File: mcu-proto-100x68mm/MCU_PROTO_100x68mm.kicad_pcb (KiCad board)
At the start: 2 copper layers, 90 x 58 mm, 836 parts, among them J1 Screw_Terminal_01x04, J2 Screw_Terminal_01x04, J3 Conn_01x01_Pin, J4 Conn_01x01_Pin

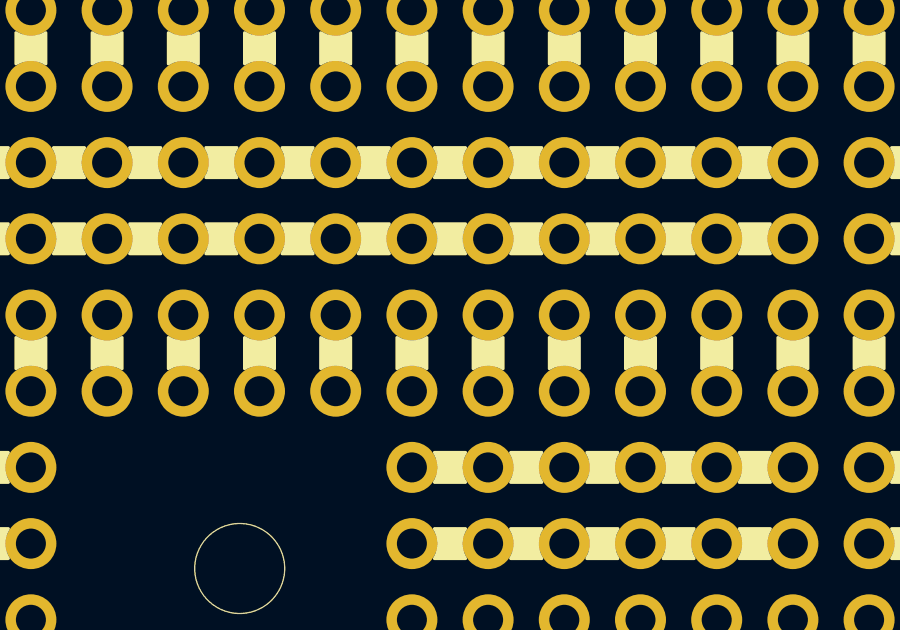
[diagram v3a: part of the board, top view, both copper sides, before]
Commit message: Silks in back plate
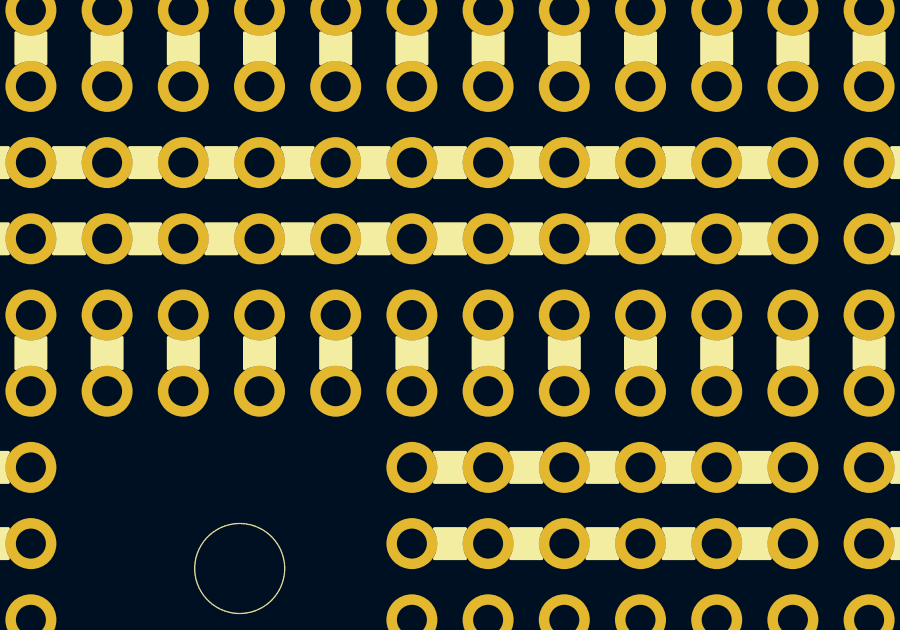
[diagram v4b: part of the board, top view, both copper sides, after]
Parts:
- added REF**310: Pad_Link_1.7mm_Width_1.0mm, proto-pcb-silks:PadLink_1.7mm_Width_1.0mm, B.Cu at (113.0, 105.5)
- added REF**311: Pad_Link_1.7mm_Width_1.0mm, proto-pcb-silks:PadLink_1.7mm_Width_1.0mm, B.Cu at (115.5, 105.5)
- added REF**312: Pad_Link_1.7mm_Width_1.0mm, proto-pcb-silks:PadLink_1.7mm_Width_1.0mm, B.Cu at (118.1, 105.5)
- added REF**318: Pad_Link_1.7mm_Width_1.0mm, proto-pcb-silks:PadLink_1.7mm_Width_1.0mm, B.Cu at (120.6, 105.5)
- added REF**353: Pad_Link_1.7mm_Width_1.0mm, proto-pcb-silks:PadLink_1.7mm_Width_1.0mm, B.Cu at (123.2, 105.5)
- added REF**354: Pad_Link_1.7mm_Width_1.0mm, proto-pcb-silks:PadLink_1.7mm_Width_1.0mm, B.Cu at (125.7, 105.5)
- added REF**355: Pad_Link_1.7mm_Width_1.0mm, proto-pcb-silks:PadLink_1.7mm_Width_1.0mm, B.Cu at (128.2, 105.5)
- added REF**356: Pad_Link_1.7mm_Width_1.0mm, proto-pcb-silks:PadLink_1.7mm_Width_1.0mm, B.Cu at (130.8, 105.5)
- added REF**357: Pad_Link_1.7mm_Width_1.0mm, proto-pcb-silks:PadLink_1.7mm_Width_1.0mm, B.Cu at (133.3, 105.5)
- added REF**358: Pad_Link_1.7mm_Width_1.0mm, proto-pcb-silks:PadLink_1.7mm_Width_1.0mm, B.Cu at (135.9, 105.5)
- added REF**359: Pad_Link_1.7mm_Width_1.0mm, proto-pcb-silks:PadLink_1.7mm_Width_1.0mm, B.Cu at (138.4, 105.5)
- added REF**360: Pad_Link_1.7mm_Width_1.0mm, proto-pcb-silks:PadLink_1.7mm_Width_1.0mm, B.Cu at (140.9, 105.5)
- added REF**361: Pad_Link_1.7mm_Width_1.0mm, proto-pcb-silks:PadLink_1.7mm_Width_1.0mm, B.Cu at (143.5, 105.5)
- added REF**362: Pad_Link_1.7mm_Width_1.0mm, proto-pcb-silks:PadLink_1.7mm_Width_1.0mm, B.Cu at (146.0, 105.5)
- added REF**363: Pad_Link_1.7mm_Width_1.0mm, proto-pcb-silks:PadLink_1.7mm_Width_1.0mm, B.Cu at (148.6, 105.5)
- added REF**364: Pad_Link_1.7mm_Width_1.0mm, proto-pcb-silks:PadLink_1.7mm_Width_1.0mm, B.Cu at (151.1, 105.5)
- added REF**365: Pad_Link_1.7mm_Width_1.0mm, proto-pcb-silks:PadLink_1.7mm_Width_1.0mm, B.Cu at (153.6, 105.5)
- added REF**366: Pad_Link_1.7mm_Width_1.0mm, proto-pcb-silks:PadLink_1.7mm_Width_1.0mm, B.Cu at (156.2, 105.5)
- added REF**367: Pad_Link_1.7mm_Width_1.0mm, proto-pcb-silks:PadLink_1.7mm_Width_1.0mm, B.Cu at (158.7, 105.5)
- added REF**368: Pad_Link_1.7mm_Width_1.0mm, proto-pcb-silks:PadLink_1.7mm_Width_1.0mm, B.Cu at (161.3, 105.5)
- added REF**369: Pad_Link_1.7mm_Width_1.0mm, proto-pcb-silks:PadLink_1.7mm_Width_1.0mm, B.Cu at (113.0, 108.0)
- added REF**370: Pad_Link_1.7mm_Width_1.0mm, proto-pcb-silks:PadLink_1.7mm_Width_1.0mm, B.Cu at (115.5, 108.0)
- added REF**371: Pad_Link_1.7mm_Width_1.0mm, proto-pcb-silks:PadLink_1.7mm_Width_1.0mm, B.Cu at (118.1, 108.0)
- added REF**372: Pad_Link_1.7mm_Width_1.0mm, proto-pcb-silks:PadLink_1.7mm_Width_1.0mm, B.Cu at (120.6, 108.0)
- added REF**373: Pad_Link_1.7mm_Width_1.0mm, proto-pcb-silks:PadLink_1.7mm_Width_1.0mm, B.Cu at (123.2, 108.0)
- added REF**374: Pad_Link_1.7mm_Width_1.0mm, proto-pcb-silks:PadLink_1.7mm_Width_1.0mm, B.Cu at (125.7, 108.0)
- added REF**375: Pad_Link_1.7mm_Width_1.0mm, proto-pcb-silks:PadLink_1.7mm_Width_1.0mm, B.Cu at (128.2, 108.0)
- added REF**376: Pad_Link_1.7mm_Width_1.0mm, proto-pcb-silks:PadLink_1.7mm_Width_1.0mm, B.Cu at (130.8, 108.0)
- added REF**377: Pad_Link_1.7mm_Width_1.0mm, proto-pcb-silks:PadLink_1.7mm_Width_1.0mm, B.Cu at (133.3, 108.0)
- added REF**378: Pad_Link_1.7mm_Width_1.0mm, proto-pcb-silks:PadLink_1.7mm_Width_1.0mm, B.Cu at (135.9, 108.0)
- added REF**379: Pad_Link_1.7mm_Width_1.0mm, proto-pcb-silks:PadLink_1.7mm_Width_1.0mm, B.Cu at (138.4, 108.0)
- added REF**380: Pad_Link_1.7mm_Width_1.0mm, proto-pcb-silks:PadLink_1.7mm_Width_1.0mm, B.Cu at (140.9, 108.0)
- added REF**381: Pad_Link_1.7mm_Width_1.0mm, proto-pcb-silks:PadLink_1.7mm_Width_1.0mm, B.Cu at (143.5, 108.0)
- added REF**382: Pad_Link_1.7mm_Width_1.0mm, proto-pcb-silks:PadLink_1.7mm_Width_1.0mm, B.Cu at (146.0, 108.0)
- added REF**383: Pad_Link_1.7mm_Width_1.0mm, proto-pcb-silks:PadLink_1.7mm_Width_1.0mm, B.Cu at (148.6, 108.0)
- added REF**384: Pad_Link_1.7mm_Width_1.0mm, proto-pcb-silks:PadLink_1.7mm_Width_1.0mm, B.Cu at (151.1, 108.0)
- added REF**385: Pad_Link_1.7mm_Width_1.0mm, proto-pcb-silks:PadLink_1.7mm_Width_1.0mm, B.Cu at (153.6, 108.0)
- added REF**386: Pad_Link_1.7mm_Width_1.0mm, proto-pcb-silks:PadLink_1.7mm_Width_1.0mm, B.Cu at (156.2, 108.0)
- added REF**387: Pad_Link_1.7mm_Width_1.0mm, proto-pcb-silks:PadLink_1.7mm_Width_1.0mm, B.Cu at (158.7, 108.0)
- added REF**388: Pad_Link_1.7mm_Width_1.0mm, proto-pcb-silks:PadLink_1.7mm_Width_1.0mm, B.Cu at (161.3, 108.0)
- added REF**389: Pad_Link_1.7mm_Width_1.0mm, proto-pcb-silks:PadLink_1.7mm_Width_1.0mm, B.Cu at (113.0, 113.1)
- added REF**390: Pad_Link_1.7mm_Width_1.0mm, proto-pcb-silks:PadLink_1.7mm_Width_1.0mm, B.Cu at (115.5, 113.1)
- added REF**391: Pad_Link_1.7mm_Width_1.0mm, proto-pcb-silks:PadLink_1.7mm_Width_1.0mm, B.Cu at (118.1, 113.1)
- added REF**392: Pad_Link_1.7mm_Width_1.0mm, proto-pcb-silks:PadLink_1.7mm_Width_1.0mm, B.Cu at (120.6, 113.1)
- added REF**393: Pad_Link_1.7mm_Width_1.0mm, proto-pcb-silks:PadLink_1.7mm_Width_1.0mm, B.Cu at (123.2, 113.1)
- added REF**394: Pad_Link_1.7mm_Width_1.0mm, proto-pcb-silks:PadLink_1.7mm_Width_1.0mm, B.Cu at (125.7, 113.1)
- added REF**395: Pad_Link_1.7mm_Width_1.0mm, proto-pcb-silks:PadLink_1.7mm_Width_1.0mm, B.Cu at (128.2, 113.1)
- added REF**396: Pad_Link_1.7mm_Width_1.0mm, proto-pcb-silks:PadLink_1.7mm_Width_1.0mm, B.Cu at (130.8, 113.1)
- added REF**397: Pad_Link_1.7mm_Width_1.0mm, proto-pcb-silks:PadLink_1.7mm_Width_1.0mm, B.Cu at (133.3, 113.1)
- added REF**398: Pad_Link_1.7mm_Width_1.0mm, proto-pcb-silks:PadLink_1.7mm_Width_1.0mm, B.Cu at (135.9, 113.1)
- added REF**399: Pad_Link_1.7mm_Width_1.0mm, proto-pcb-silks:PadLink_1.7mm_Width_1.0mm, B.Cu at (138.4, 113.1)
- added REF**400: Pad_Link_1.7mm_Width_1.0mm, proto-pcb-silks:PadLink_1.7mm_Width_1.0mm, B.Cu at (140.9, 113.1)
- added REF**401: Pad_Link_1.7mm_Width_1.0mm, proto-pcb-silks:PadLink_1.7mm_Width_1.0mm, B.Cu at (143.5, 113.1)
- added REF**402: Pad_Link_1.7mm_Width_1.0mm, proto-pcb-silks:PadLink_1.7mm_Width_1.0mm, B.Cu at (146.0, 113.1)
- added REF**403: Pad_Link_1.7mm_Width_1.0mm, proto-pcb-silks:PadLink_1.7mm_Width_1.0mm, B.Cu at (148.6, 113.1)
- added REF**404: Pad_Link_1.7mm_Width_1.0mm, proto-pcb-silks:PadLink_1.7mm_Width_1.0mm, B.Cu at (151.1, 113.1)
- added REF**405: Pad_Link_1.7mm_Width_1.0mm, proto-pcb-silks:PadLink_1.7mm_Width_1.0mm, B.Cu at (153.6, 113.1)
- added REF**406: Pad_Link_1.7mm_Width_1.0mm, proto-pcb-silks:PadLink_1.7mm_Width_1.0mm, B.Cu at (156.2, 113.1)
- added REF**407: Pad_Link_1.7mm_Width_1.0mm, proto-pcb-silks:PadLink_1.7mm_Width_1.0mm, B.Cu at (158.7, 113.1)
- added REF**408: Pad_Link_1.7mm_Width_1.0mm, proto-pcb-silks:PadLink_1.7mm_Width_1.0mm, B.Cu at (161.3, 113.1)
- added REF**409: Pad_Link_1.7mm_Width_1.0mm, proto-pcb-silks:PadLink_1.7mm_Width_1.0mm, B.Cu at (113.0, 115.6)
- added REF**410: Pad_Link_1.7mm_Width_1.0mm, proto-pcb-silks:PadLink_1.7mm_Width_1.0mm, B.Cu at (115.5, 115.6)
- added REF**411: Pad_Link_1.7mm_Width_1.0mm, proto-pcb-silks:PadLink_1.7mm_Width_1.0mm, B.Cu at (118.1, 115.6)
- added REF**412: Pad_Link_1.7mm_Width_1.0mm, proto-pcb-silks:PadLink_1.7mm_Width_1.0mm, B.Cu at (120.6, 115.6)
- added REF**413: Pad_Link_1.7mm_Width_1.0mm, proto-pcb-silks:PadLink_1.7mm_Width_1.0mm, B.Cu at (123.2, 115.6)
- added REF**414: Pad_Link_1.7mm_Width_1.0mm, proto-pcb-silks:PadLink_1.7mm_Width_1.0mm, B.Cu at (125.7, 115.6)
- added REF**415: Pad_Link_1.7mm_Width_1.0mm, proto-pcb-silks:PadLink_1.7mm_Width_1.0mm, B.Cu at (128.2, 115.6)
- added REF**416: Pad_Link_1.7mm_Width_1.0mm, proto-pcb-silks:PadLink_1.7mm_Width_1.0mm, B.Cu at (130.8, 115.6)
- added REF**417: Pad_Link_1.7mm_Width_1.0mm, proto-pcb-silks:PadLink_1.7mm_Width_1.0mm, B.Cu at (133.3, 115.6)
- added REF**418: Pad_Link_1.7mm_Width_1.0mm, proto-pcb-silks:PadLink_1.7mm_Width_1.0mm, B.Cu at (135.9, 115.6)
- added REF**419: Pad_Link_1.7mm_Width_1.0mm, proto-pcb-silks:PadLink_1.7mm_Width_1.0mm, B.Cu at (138.4, 115.6)
- added REF**420: Pad_Link_1.7mm_Width_1.0mm, proto-pcb-silks:PadLink_1.7mm_Width_1.0mm, B.Cu at (113.0, 123.2)
- added REF**421: Pad_Link_1.7mm_Width_1.0mm, proto-pcb-silks:PadLink_1.7mm_Width_1.0mm, B.Cu at (143.5, 115.6)
- added REF**422: Pad_Link_1.7mm_Width_1.0mm, proto-pcb-silks:PadLink_1.7mm_Width_1.0mm, B.Cu at (146.0, 115.6)
- added REF**423: Pad_Link_1.7mm_Width_1.0mm, proto-pcb-silks:PadLink_1.7mm_Width_1.0mm, B.Cu at (148.6, 115.6)
- added REF**424: Pad_Link_1.7mm_Width_1.0mm, proto-pcb-silks:PadLink_1.7mm_Width_1.0mm, B.Cu at (151.1, 115.6)
- added REF**425: Pad_Link_1.7mm_Width_1.0mm, proto-pcb-silks:PadLink_1.7mm_Width_1.0mm, B.Cu at (153.6, 115.6)
- added REF**426: Pad_Link_1.7mm_Width_1.0mm, proto-pcb-silks:PadLink_1.7mm_Width_1.0mm, B.Cu at (156.2, 115.6)
- added REF**427: Pad_Link_1.7mm_Width_1.0mm, proto-pcb-silks:PadLink_1.7mm_Width_1.0mm, B.Cu at (158.7, 115.6)
- added REF**428: Pad_Link_1.7mm_Width_1.0mm, proto-pcb-silks:PadLink_1.7mm_Width_1.0mm, B.Cu at (161.3, 115.6)
- added REF**429: Pad_Link_1.7mm_Width_1.0mm, proto-pcb-silks:PadLink_1.7mm_Width_1.0mm, B.Cu at (163.8, 115.6)
- added REF**430: Pad_Link_1.7mm_Width_1.0mm, proto-pcb-silks:PadLink_1.7mm_Width_1.0mm, B.Cu at (166.3, 115.6)
- added REF**431: Pad_Link_1.7mm_Width_1.0mm, proto-pcb-silks:PadLink_1.7mm_Width_1.0mm, B.Cu at (113.0, 118.2)
- added REF**432: Pad_Link_1.7mm_Width_1.0mm, proto-pcb-silks:PadLink_1.7mm_Width_1.0mm, B.Cu at (115.5, 118.2)
- added REF**433: Pad_Link_1.7mm_Width_1.0mm, proto-pcb-silks:PadLink_1.7mm_Width_1.0mm, B.Cu at (118.1, 118.2)
- added REF**434: Pad_Link_1.7mm_Width_1.0mm, proto-pcb-silks:PadLink_1.7mm_Width_1.0mm, B.Cu at (120.6, 118.2)
- added REF**435: Pad_Link_1.7mm_Width_1.0mm, proto-pcb-silks:PadLink_1.7mm_Width_1.0mm, B.Cu at (123.2, 118.2)
- added REF**436: Pad_Link_1.7mm_Width_1.0mm, proto-pcb-silks:PadLink_1.7mm_Width_1.0mm, B.Cu at (125.7, 118.2)
- added REF**437: Pad_Link_1.7mm_Width_1.0mm, proto-pcb-silks:PadLink_1.7mm_Width_1.0mm, B.Cu at (128.2, 118.2)
- added REF**438: Pad_Link_1.7mm_Width_1.0mm, proto-pcb-silks:PadLink_1.7mm_Width_1.0mm, B.Cu at (130.8, 118.2)
- added REF**439: Pad_Link_1.7mm_Width_1.0mm, proto-pcb-silks:PadLink_1.7mm_Width_1.0mm, B.Cu at (133.3, 118.2)
- added REF**440: Pad_Link_1.7mm_Width_1.0mm, proto-pcb-silks:PadLink_1.7mm_Width_1.0mm, B.Cu at (135.9, 118.2)
- added REF**441: Pad_Link_1.7mm_Width_1.0mm, proto-pcb-silks:PadLink_1.7mm_Width_1.0mm, B.Cu at (138.4, 118.2)
- added REF**442: Pad_Link_1.7mm_Width_1.0mm, proto-pcb-silks:PadLink_1.7mm_Width_1.0mm, B.Cu at (115.5, 123.2)
- added REF**443: Pad_Link_1.7mm_Width_1.0mm, proto-pcb-silks:PadLink_1.7mm_Width_1.0mm, B.Cu at (143.5, 118.2)
- added REF**444: Pad_Link_1.7mm_Width_1.0mm, proto-pcb-silks:PadLink_1.7mm_Width_1.0mm, B.Cu at (146.0, 118.2)
- added REF**445: Pad_Link_1.7mm_Width_1.0mm, proto-pcb-silks:PadLink_1.7mm_Width_1.0mm, B.Cu at (148.6, 118.2)
- added REF**446: Pad_Link_1.7mm_Width_1.0mm, proto-pcb-silks:PadLink_1.7mm_Width_1.0mm, B.Cu at (151.1, 118.2)
- added REF**447: Pad_Link_1.7mm_Width_1.0mm, proto-pcb-silks:PadLink_1.7mm_Width_1.0mm, B.Cu at (153.6, 118.2)
- added REF**448: Pad_Link_1.7mm_Width_1.0mm, proto-pcb-silks:PadLink_1.7mm_Width_1.0mm, B.Cu at (156.2, 118.2)
- added REF**449: Pad_Link_1.7mm_Width_1.0mm, proto-pcb-silks:PadLink_1.7mm_Width_1.0mm, B.Cu at (158.7, 118.2)
- added REF**450: Pad_Link_1.7mm_Width_1.0mm, proto-pcb-silks:PadLink_1.7mm_Width_1.0mm, B.Cu at (161.3, 118.2)
- added REF**451: Pad_Link_1.7mm_Width_1.0mm, proto-pcb-silks:PadLink_1.7mm_Width_1.0mm, B.Cu at (163.8, 118.2)
- added REF**452: Pad_Link_1.7mm_Width_1.0mm, proto-pcb-silks:PadLink_1.7mm_Width_1.0mm, B.Cu at (166.3, 118.2)
- added REF**453: Pad_Link_1.7mm_Width_1.0mm, proto-pcb-silks:PadLink_1.7mm_Width_1.0mm, B.Cu at (118.1, 123.2)
- added REF**454: Pad_Link_1.7mm_Width_1.0mm, proto-pcb-silks:PadLink_1.7mm_Width_1.0mm, B.Cu at (120.6, 123.2)
- added REF**455: Pad_Link_1.7mm_Width_1.0mm, proto-pcb-silks:PadLink_1.7mm_Width_1.0mm, B.Cu at (123.2, 123.2)
- added REF**456: Pad_Link_1.7mm_Width_1.0mm, proto-pcb-silks:PadLink_1.7mm_Width_1.0mm, B.Cu at (125.7, 123.2)
- added REF**457: Pad_Link_1.7mm_Width_1.0mm, proto-pcb-silks:PadLink_1.7mm_Width_1.0mm, B.Cu at (128.2, 123.2)
- added REF**458: Pad_Link_1.7mm_Width_1.0mm, proto-pcb-silks:PadLink_1.7mm_Width_1.0mm, B.Cu at (130.8, 123.2)
- added REF**459: Pad_Link_1.7mm_Width_1.0mm, proto-pcb-silks:PadLink_1.7mm_Width_1.0mm, B.Cu at (133.3, 123.2)
- added REF**460: Pad_Link_1.7mm_Width_1.0mm, proto-pcb-silks:PadLink_1.7mm_Width_1.0mm, B.Cu at (135.9, 123.2)
- added REF**461: Pad_Link_1.7mm_Width_1.0mm, proto-pcb-silks:PadLink_1.7mm_Width_1.0mm, B.Cu at (138.4, 123.2)
- added REF**462: Pad_Link_1.7mm_Width_1.0mm, proto-pcb-silks:PadLink_1.7mm_Width_1.0mm, B.Cu at (140.9, 123.2)
- added REF**463: Pad_Link_1.7mm_Width_1.0mm, proto-pcb-silks:PadLink_1.7mm_Width_1.0mm, B.Cu at (143.5, 123.2)
- added REF**464: Pad_Link_1.7mm_Width_1.0mm, proto-pcb-silks:PadLink_1.7mm_Width_1.0mm, B.Cu at (146.0, 123.2)
- added REF**465: Pad_Link_1.7mm_Width_1.0mm, proto-pcb-silks:PadLink_1.7mm_Width_1.0mm, B.Cu at (148.6, 123.2)
- added REF**466: Pad_Link_1.7mm_Width_1.0mm, proto-pcb-silks:PadLink_1.7mm_Width_1.0mm, B.Cu at (151.1, 123.2)
- added REF**467: Pad_Link_1.7mm_Width_1.0mm, proto-pcb-silks:PadLink_1.7mm_Width_1.0mm, B.Cu at (153.6, 123.2)
- added REF**468: Pad_Link_1.7mm_Width_1.0mm, proto-pcb-silks:PadLink_1.7mm_Width_1.0mm, B.Cu at (156.2, 123.2)
- added REF**469: Pad_Link_1.7mm_Width_1.0mm, proto-pcb-silks:PadLink_1.7mm_Width_1.0mm, B.Cu at (158.7, 123.2)
- added REF**470: Pad_Link_1.7mm_Width_1.0mm, proto-pcb-silks:PadLink_1.7mm_Width_1.0mm, B.Cu at (161.3, 123.2)
- added REF**471: Pad_Link_1.7mm_Width_1.0mm, proto-pcb-silks:PadLink_1.7mm_Width_1.0mm, B.Cu at (163.8, 123.2)
- added REF**472: Pad_Link_1.7mm_Width_1.0mm, proto-pcb-silks:PadLink_1.7mm_Width_1.0mm, B.Cu at (166.3, 123.2)
- added REF**473: Pad_Link_1.7mm_Width_1.0mm, proto-pcb-silks:PadLink_1.7mm_Width_1.0mm, B.Cu at (168.9, 123.2)
- added REF**474: Pad_Link_1.7mm_Width_1.0mm, proto-pcb-silks:PadLink_1.7mm_Width_1.0mm, B.Cu at (113.0, 125.8)
- added REF**475: Pad_Link_1.7mm_Width_1.0mm, proto-pcb-silks:PadLink_1.7mm_Width_1.0mm, B.Cu at (115.5, 125.8)
- added REF**476: Pad_Link_1.7mm_Width_1.0mm, proto-pcb-silks:PadLink_1.7mm_Width_1.0mm, B.Cu at (118.1, 125.8)
- added REF**477: Pad_Link_1.7mm_Width_1.0mm, proto-pcb-silks:PadLink_1.7mm_Width_1.0mm, B.Cu at (120.6, 125.8)
- added REF**478: Pad_Link_1.7mm_Width_1.0mm, proto-pcb-silks:PadLink_1.7mm_Width_1.0mm, B.Cu at (123.2, 125.8)
- added REF**479: Pad_Link_1.7mm_Width_1.0mm, proto-pcb-silks:PadLink_1.7mm_Width_1.0mm, B.Cu at (125.7, 125.8)
- added REF**480: Pad_Link_1.7mm_Width_1.0mm, proto-pcb-silks:PadLink_1.7mm_Width_1.0mm, B.Cu at (128.2, 125.8)
- added REF**481: Pad_Link_1.7mm_Width_1.0mm, proto-pcb-silks:PadLink_1.7mm_Width_1.0mm, B.Cu at (130.8, 125.8)
- added REF**482: Pad_Link_1.7mm_Width_1.0mm, proto-pcb-silks:PadLink_1.7mm_Width_1.0mm, B.Cu at (133.3, 125.8)
- added REF**483: Pad_Link_1.7mm_Width_1.0mm, proto-pcb-silks:PadLink_1.7mm_Width_1.0mm, B.Cu at (135.9, 125.8)
- added REF**484: Pad_Link_1.7mm_Width_1.0mm, proto-pcb-silks:PadLink_1.7mm_Width_1.0mm, B.Cu at (138.4, 125.8)
- added REF**485: Pad_Link_1.7mm_Width_1.0mm, proto-pcb-silks:PadLink_1.7mm_Width_1.0mm, B.Cu at (140.9, 125.8)
- added REF**486: Pad_Link_1.7mm_Width_1.0mm, proto-pcb-silks:PadLink_1.7mm_Width_1.0mm, B.Cu at (143.5, 125.8)
- added REF**487: Pad_Link_1.7mm_Width_1.0mm, proto-pcb-silks:PadLink_1.7mm_Width_1.0mm, B.Cu at (146.0, 125.8)
- added REF**488: Pad_Link_1.7mm_Width_1.0mm, proto-pcb-silks:PadLink_1.7mm_Width_1.0mm, B.Cu at (148.6, 125.8)
- added REF**489: Pad_Link_1.7mm_Width_1.0mm, proto-pcb-silks:PadLink_1.7mm_Width_1.0mm, B.Cu at (151.1, 125.8)
- added REF**490: Pad_Link_1.7mm_Width_1.0mm, proto-pcb-silks:PadLink_1.7mm_Width_1.0mm, B.Cu at (153.6, 125.8)
- added REF**491: Pad_Link_1.7mm_Width_1.0mm, proto-pcb-silks:PadLink_1.7mm_Width_1.0mm, B.Cu at (156.2, 125.8)
- added REF**492: Pad_Link_1.7mm_Width_1.0mm, proto-pcb-silks:PadLink_1.7mm_Width_1.0mm, B.Cu at (158.7, 125.8)
- added REF**493: Pad_Link_1.7mm_Width_1.0mm, proto-pcb-silks:PadLink_1.7mm_Width_1.0mm, B.Cu at (161.3, 125.8)
- added REF**494: Pad_Link_1.7mm_Width_1.0mm, proto-pcb-silks:PadLink_1.7mm_Width_1.0mm, B.Cu at (163.8, 125.8)
- added REF**495: Pad_Link_1.7mm_Width_1.0mm, proto-pcb-silks:PadLink_1.7mm_Width_1.0mm, B.Cu at (166.3, 125.8)
- added REF**496: Pad_Link_1.7mm_Width_1.0mm, proto-pcb-silks:PadLink_1.7mm_Width_1.0mm, B.Cu at (168.9, 125.8)
- added REF**497: Pad_Link_1.7mm_Width_1.0mm, proto-pcb-silks:PadLink_1.7mm_Width_1.0mm, B.Cu at (113.0, 128.3)
- added REF**498: Pad_Link_1.7mm_Width_1.0mm, proto-pcb-silks:PadLink_1.7mm_Width_1.0mm, B.Cu at (115.5, 128.3)
- added REF**499: Pad_Link_1.7mm_Width_1.0mm, proto-pcb-silks:PadLink_1.7mm_Width_1.0mm, B.Cu at (118.1, 128.3)
- added REF**500: Pad_Link_1.7mm_Width_1.0mm, proto-pcb-silks:PadLink_1.7mm_Width_1.0mm, B.Cu at (120.6, 128.3)
- added REF**501: Pad_Link_1.7mm_Width_1.0mm, proto-pcb-silks:PadLink_1.7mm_Width_1.0mm, B.Cu at (123.2, 128.3)
- added REF**502: Pad_Link_1.7mm_Width_1.0mm, proto-pcb-silks:PadLink_1.7mm_Width_1.0mm, B.Cu at (125.7, 128.3)
- added REF**503: Pad_Link_1.7mm_Width_1.0mm, proto-pcb-silks:PadLink_1.7mm_Width_1.0mm, B.Cu at (128.2, 128.3)
- added REF**504: Pad_Link_1.7mm_Width_1.0mm, proto-pcb-silks:PadLink_1.7mm_Width_1.0mm, B.Cu at (130.8, 128.3)
- added REF**505: Pad_Link_1.7mm_Width_1.0mm, proto-pcb-silks:PadLink_1.7mm_Width_1.0mm, B.Cu at (133.3, 128.3)
- added REF**506: Pad_Link_1.7mm_Width_1.0mm, proto-pcb-silks:PadLink_1.7mm_Width_1.0mm, B.Cu at (135.9, 128.3)
- added REF**507: Pad_Link_1.7mm_Width_1.0mm, proto-pcb-silks:PadLink_1.7mm_Width_1.0mm, B.Cu at (138.4, 128.3)
- added REF**508: Pad_Link_1.7mm_Width_1.0mm, proto-pcb-silks:PadLink_1.7mm_Width_1.0mm, B.Cu at (140.9, 128.3)
- added REF**509: Pad_Link_1.7mm_Width_1.0mm, proto-pcb-silks:PadLink_1.7mm_Width_1.0mm, B.Cu at (143.5, 128.3)
- added REF**510: Pad_Link_1.7mm_Width_1.0mm, proto-pcb-silks:PadLink_1.7mm_Width_1.0mm, B.Cu at (146.0, 128.3)
- added REF**511: Pad_Link_1.7mm_Width_1.0mm, proto-pcb-silks:PadLink_1.7mm_Width_1.0mm, B.Cu at (148.6, 128.3)
- added REF**512: Pad_Link_1.7mm_Width_1.0mm, proto-pcb-silks:PadLink_1.7mm_Width_1.0mm, B.Cu at (151.1, 128.3)
- added REF**513: Pad_Link_1.7mm_Width_1.0mm, proto-pcb-silks:PadLink_1.7mm_Width_1.0mm, B.Cu at (153.6, 128.3)
- added REF**514: Pad_Link_1.7mm_Width_1.0mm, proto-pcb-silks:PadLink_1.7mm_Width_1.0mm, B.Cu at (156.2, 128.3)
- added REF**515: Pad_Link_1.7mm_Width_1.0mm, proto-pcb-silks:PadLink_1.7mm_Width_1.0mm, B.Cu at (158.7, 128.3)
- added REF**516: Pad_Link_1.7mm_Width_1.0mm, proto-pcb-silks:PadLink_1.7mm_Width_1.0mm, B.Cu at (161.3, 128.3)
- added REF**517: Pad_Link_1.7mm_Width_1.0mm, proto-pcb-silks:PadLink_1.7mm_Width_1.0mm, B.Cu at (163.8, 128.3)
- added REF**518: Pad_Link_1.7mm_Width_1.0mm, proto-pcb-silks:PadLink_1.7mm_Width_1.0mm, B.Cu at (166.3, 128.3)
- added REF**519: Pad_Link_1.7mm_Width_1.0mm, proto-pcb-silks:PadLink_1.7mm_Width_1.0mm, B.Cu at (168.9, 128.3)
- added REF**520: Pad_Link_1.7mm_Width_1.0mm, proto-pcb-silks:PadLink_1.7mm_Width_1.0mm, B.Cu at (113.0, 130.8)
- added REF**521: Pad_Link_1.7mm_Width_1.0mm, proto-pcb-silks:PadLink_1.7mm_Width_1.0mm, B.Cu at (115.5, 130.8)
- added REF**522: Pad_Link_1.7mm_Width_1.0mm, proto-pcb-silks:PadLink_1.7mm_Width_1.0mm, B.Cu at (118.1, 130.8)
- added REF**523: Pad_Link_1.7mm_Width_1.0mm, proto-pcb-silks:PadLink_1.7mm_Width_1.0mm, B.Cu at (120.6, 130.8)
- added REF**524: Pad_Link_1.7mm_Width_1.0mm, proto-pcb-silks:PadLink_1.7mm_Width_1.0mm, B.Cu at (123.2, 130.8)
- added REF**525: Pad_Link_1.7mm_Width_1.0mm, proto-pcb-silks:PadLink_1.7mm_Width_1.0mm, B.Cu at (125.7, 130.8)
- added REF**526: Pad_Link_1.7mm_Width_1.0mm, proto-pcb-silks:PadLink_1.7mm_Width_1.0mm, B.Cu at (128.2, 130.8)
- added REF**527: Pad_Link_1.7mm_Width_1.0mm, proto-pcb-silks:PadLink_1.7mm_Width_1.0mm, B.Cu at (130.8, 130.8)
- added REF**528: Pad_Link_1.7mm_Width_1.0mm, proto-pcb-silks:PadLink_1.7mm_Width_1.0mm, B.Cu at (133.3, 130.8)
- added REF**529: Pad_Link_1.7mm_Width_1.0mm, proto-pcb-silks:PadLink_1.7mm_Width_1.0mm, B.Cu at (135.9, 130.8)
- added REF**530: Pad_Link_1.7mm_Width_1.0mm, proto-pcb-silks:PadLink_1.7mm_Width_1.0mm, B.Cu at (138.4, 130.8)
- added REF**531: Pad_Link_1.7mm_Width_1.0mm, proto-pcb-silks:PadLink_1.7mm_Width_1.0mm, B.Cu at (140.9, 130.8)
- added REF**532: Pad_Link_1.7mm_Width_1.0mm, proto-pcb-silks:PadLink_1.7mm_Width_1.0mm, B.Cu at (143.5, 130.8)
- added REF**533: Pad_Link_1.7mm_Width_1.0mm, proto-pcb-silks:PadLink_1.7mm_Width_1.0mm, B.Cu at (146.0, 130.8)
- added REF**534: Pad_Link_1.7mm_Width_1.0mm, proto-pcb-silks:PadLink_1.7mm_Width_1.0mm, B.Cu at (148.6, 130.8)
- added REF**535: Pad_Link_1.7mm_Width_1.0mm, proto-pcb-silks:PadLink_1.7mm_Width_1.0mm, B.Cu at (151.1, 130.8)
- added REF**536: Pad_Link_1.7mm_Width_1.0mm, proto-pcb-silks:PadLink_1.7mm_Width_1.0mm, B.Cu at (153.6, 130.8)
- added REF**537: Pad_Link_1.7mm_Width_1.0mm, proto-pcb-silks:PadLink_1.7mm_Width_1.0mm, B.Cu at (156.2, 130.8)
- added REF**538: Pad_Link_1.7mm_Width_1.0mm, proto-pcb-silks:PadLink_1.7mm_Width_1.0mm, B.Cu at (158.7, 130.8)
- added REF**539: Pad_Link_1.7mm_Width_1.0mm, proto-pcb-silks:PadLink_1.7mm_Width_1.0mm, B.Cu at (161.3, 130.8)
- added REF**540: Pad_Link_1.7mm_Width_1.0mm, proto-pcb-silks:PadLink_1.7mm_Width_1.0mm, B.Cu at (163.8, 130.8)
- added REF**541: Pad_Link_1.7mm_Width_1.0mm, proto-pcb-silks:PadLink_1.7mm_Width_1.0mm, B.Cu at (166.3, 130.8)
- added REF**542: Pad_Link_1.7mm_Width_1.0mm, proto-pcb-silks:PadLink_1.7mm_Width_1.0mm, B.Cu at (168.9, 130.8)
- added REF**543: Pad_Link_1.7mm_Width_1.0mm, proto-pcb-silks:PadLink_1.7mm_Width_1.0mm, B.Cu at (113.0, 133.4)
- added REF**544: Pad_Link_1.7mm_Width_1.0mm, proto-pcb-silks:PadLink_1.7mm_Width_1.0mm, B.Cu at (115.5, 133.4)
- added REF**545: Pad_Link_1.7mm_Width_1.0mm, proto-pcb-silks:PadLink_1.7mm_Width_1.0mm, B.Cu at (118.1, 133.4)
- added REF**546: Pad_Link_1.7mm_Width_1.0mm, proto-pcb-silks:PadLink_1.7mm_Width_1.0mm, B.Cu at (120.6, 133.4)
- added REF**547: Pad_Link_1.7mm_Width_1.0mm, proto-pcb-silks:PadLink_1.7mm_Width_1.0mm, B.Cu at (123.2, 133.4)
- added REF**548: Pad_Link_1.7mm_Width_1.0mm, proto-pcb-silks:PadLink_1.7mm_Width_1.0mm, B.Cu at (125.7, 133.4)
- added REF**549: Pad_Link_1.7mm_Width_1.0mm, proto-pcb-silks:PadLink_1.7mm_Width_1.0mm, B.Cu at (128.2, 133.4)
- added REF**550: Pad_Link_1.7mm_Width_1.0mm, proto-pcb-silks:PadLink_1.7mm_Width_1.0mm, B.Cu at (130.8, 133.4)
- added REF**551: Pad_Link_1.7mm_Width_1.0mm, proto-pcb-silks:PadLink_1.7mm_Width_1.0mm, B.Cu at (133.3, 133.4)
- added REF**552: Pad_Link_1.7mm_Width_1.0mm, proto-pcb-silks:PadLink_1.7mm_Width_1.0mm, B.Cu at (135.9, 133.4)
- added REF**553: Pad_Link_1.7mm_Width_1.0mm, proto-pcb-silks:PadLink_1.7mm_Width_1.0mm, B.Cu at (138.4, 133.4)
- added REF**554: Pad_Link_1.7mm_Width_1.0mm, proto-pcb-silks:PadLink_1.7mm_Width_1.0mm, B.Cu at (140.9, 133.4)
- added REF**555: Pad_Link_1.7mm_Width_1.0mm, proto-pcb-silks:PadLink_1.7mm_Width_1.0mm, B.Cu at (143.5, 133.4)
- added REF**556: Pad_Link_1.7mm_Width_1.0mm, proto-pcb-silks:PadLink_1.7mm_Width_1.0mm, B.Cu at (146.0, 133.4)
- added REF**557: Pad_Link_1.7mm_Width_1.0mm, proto-pcb-silks:PadLink_1.7mm_Width_1.0mm, B.Cu at (148.6, 133.4)
- added REF**558: Pad_Link_1.7mm_Width_1.0mm, proto-pcb-silks:PadLink_1.7mm_Width_1.0mm, B.Cu at (151.1, 133.4)
- added REF**559: Pad_Link_1.7mm_Width_1.0mm, proto-pcb-silks:PadLink_1.7mm_Width_1.0mm, B.Cu at (153.6, 133.4)
- added REF**560: Pad_Link_1.7mm_Width_1.0mm, proto-pcb-silks:PadLink_1.7mm_Width_1.0mm, B.Cu at (156.2, 133.4)
- added REF**561: Pad_Link_1.7mm_Width_1.0mm, proto-pcb-silks:PadLink_1.7mm_Width_1.0mm, B.Cu at (158.7, 133.4)
- added REF**562: Pad_Link_1.7mm_Width_1.0mm, proto-pcb-silks:PadLink_1.7mm_Width_1.0mm, B.Cu at (161.3, 133.4)
- added REF**563: Pad_Link_1.7mm_Width_1.0mm, proto-pcb-silks:PadLink_1.7mm_Width_1.0mm, B.Cu at (163.8, 133.4)
- added REF**564: Pad_Link_1.7mm_Width_1.0mm, proto-pcb-silks:PadLink_1.7mm_Width_1.0mm, B.Cu at (166.3, 133.4)
- added REF**565: Pad_Link_1.7mm_Width_1.0mm, proto-pcb-silks:PadLink_1.7mm_Width_1.0mm, B.Cu at (168.9, 133.4)
- added REF**566: Pad_Link_1.7mm_Width_1.0mm, proto-pcb-silks:PadLink_1.7mm_Width_1.0mm, B.Cu at (113.0, 135.9)
- added REF**567: Pad_Link_1.7mm_Width_1.0mm, proto-pcb-silks:PadLink_1.7mm_Width_1.0mm, B.Cu at (115.5, 135.9)
- added REF**568: Pad_Link_1.7mm_Width_1.0mm, proto-pcb-silks:PadLink_1.7mm_Width_1.0mm, B.Cu at (118.1, 135.9)
- added REF**569: Pad_Link_1.7mm_Width_1.0mm, proto-pcb-silks:PadLink_1.7mm_Width_1.0mm, B.Cu at (120.6, 135.9)
- added REF**570: Pad_Link_1.7mm_Width_1.0mm, proto-pcb-silks:PadLink_1.7mm_Width_1.0mm, B.Cu at (123.2, 135.9)
- added REF**571: Pad_Link_1.7mm_Width_1.0mm, proto-pcb-silks:PadLink_1.7mm_Width_1.0mm, B.Cu at (125.7, 135.9)
- added REF**572: Pad_Link_1.7mm_Width_1.0mm, proto-pcb-silks:PadLink_1.7mm_Width_1.0mm, B.Cu at (128.2, 135.9)
- added REF**573: Pad_Link_1.7mm_Width_1.0mm, proto-pcb-silks:PadLink_1.7mm_Width_1.0mm, B.Cu at (130.8, 135.9)
- added REF**574: Pad_Link_1.7mm_Width_1.0mm, proto-pcb-silks:PadLink_1.7mm_Width_1.0mm, B.Cu at (133.3, 135.9)
- added REF**575: Pad_Link_1.7mm_Width_1.0mm, proto-pcb-silks:PadLink_1.7mm_Width_1.0mm, B.Cu at (135.9, 135.9)
- added REF**576: Pad_Link_1.7mm_Width_1.0mm, proto-pcb-silks:PadLink_1.7mm_Width_1.0mm, B.Cu at (138.4, 135.9)
- added REF**577: Pad_Link_1.7mm_Width_1.0mm, proto-pcb-silks:PadLink_1.7mm_Width_1.0mm, B.Cu at (140.9, 135.9)
- added REF**578: Pad_Link_1.7mm_Width_1.0mm, proto-pcb-silks:PadLink_1.7mm_Width_1.0mm, B.Cu at (143.5, 135.9)
- added REF**579: Pad_Link_1.7mm_Width_1.0mm, proto-pcb-silks:PadLink_1.7mm_Width_1.0mm, B.Cu at (146.0, 135.9)
- added REF**580: Pad_Link_1.7mm_Width_1.0mm, proto-pcb-silks:PadLink_1.7mm_Width_1.0mm, B.Cu at (148.6, 135.9)
- added REF**581: Pad_Link_1.7mm_Width_1.0mm, proto-pcb-silks:PadLink_1.7mm_Width_1.0mm, B.Cu at (151.1, 135.9)
- added REF**582: Pad_Link_1.7mm_Width_1.0mm, proto-pcb-silks:PadLink_1.7mm_Width_1.0mm, B.Cu at (153.6, 135.9)
- added REF**583: Pad_Link_1.7mm_Width_1.0mm, proto-pcb-silks:PadLink_1.7mm_Width_1.0mm, B.Cu at (156.2, 135.9)
- added REF**584: Pad_Link_1.7mm_Width_1.0mm, proto-pcb-silks:PadLink_1.7mm_Width_1.0mm, B.Cu at (158.7, 135.9)
- added REF**585: Pad_Link_1.7mm_Width_1.0mm, proto-pcb-silks:PadLink_1.7mm_Width_1.0mm, B.Cu at (161.3, 135.9)
- added REF**586: Pad_Link_1.7mm_Width_1.0mm, proto-pcb-silks:PadLink_1.7mm_Width_1.0mm, B.Cu at (163.8, 135.9)
- added REF**587: Pad_Link_1.7mm_Width_1.0mm, proto-pcb-silks:PadLink_1.7mm_Width_1.0mm, B.Cu at (166.3, 135.9)
- added REF**588: Pad_Link_1.7mm_Width_1.0mm, proto-pcb-silks:PadLink_1.7mm_Width_1.0mm, B.Cu at (168.9, 135.9)
- added REF**589: Pad_Link_1.7mm_Width_1.0mm, proto-pcb-silks:PadLink_1.7mm_Width_1.0mm, B.Cu at (113.0, 138.5)
- added REF**590: Pad_Link_1.7mm_Width_1.0mm, proto-pcb-silks:PadLink_1.7mm_Width_1.0mm, B.Cu at (115.5, 138.5)
- added REF**591: Pad_Link_1.7mm_Width_1.0mm, proto-pcb-silks:PadLink_1.7mm_Width_1.0mm, B.Cu at (118.1, 138.5)
- added REF**592: Pad_Link_1.7mm_Width_1.0mm, proto-pcb-silks:PadLink_1.7mm_Width_1.0mm, B.Cu at (120.6, 138.5)
- added REF**593: Pad_Link_1.7mm_Width_1.0mm, proto-pcb-silks:PadLink_1.7mm_Width_1.0mm, B.Cu at (123.2, 138.5)
- added REF**594: Pad_Link_1.7mm_Width_1.0mm, proto-pcb-silks:PadLink_1.7mm_Width_1.0mm, B.Cu at (125.7, 138.5)
- added REF**595: Pad_Link_1.7mm_Width_1.0mm, proto-pcb-silks:PadLink_1.7mm_Width_1.0mm, B.Cu at (128.2, 138.5)
- added REF**596: Pad_Link_1.7mm_Width_1.0mm, proto-pcb-silks:PadLink_1.7mm_Width_1.0mm, B.Cu at (130.8, 138.5)
- added REF**597: Pad_Link_1.7mm_Width_1.0mm, proto-pcb-silks:PadLink_1.7mm_Width_1.0mm, B.Cu at (133.3, 138.5)
- added REF**598: Pad_Link_1.7mm_Width_1.0mm, proto-pcb-silks:PadLink_1.7mm_Width_1.0mm, B.Cu at (135.9, 138.5)
- added REF**599: Pad_Link_1.7mm_Width_1.0mm, proto-pcb-silks:PadLink_1.7mm_Width_1.0mm, B.Cu at (138.4, 138.5)
- added REF**601: Pad_Link_1.7mm_Width_1.0mm, proto-pcb-silks:PadLink_1.7mm_Width_1.0mm, B.Cu at (143.5, 138.5)
- added REF**602: Pad_Link_1.7mm_Width_1.0mm, proto-pcb-silks:PadLink_1.7mm_Width_1.0mm, B.Cu at (146.0, 138.5)
- added REF**603: Pad_Link_1.7mm_Width_1.0mm, proto-pcb-silks:PadLink_1.7mm_Width_1.0mm, B.Cu at (148.6, 138.5)
- added REF**604: Pad_Link_1.7mm_Width_1.0mm, proto-pcb-silks:PadLink_1.7mm_Width_1.0mm, B.Cu at (151.1, 138.5)
- added REF**605: Pad_Link_1.7mm_Width_1.0mm, proto-pcb-silks:PadLink_1.7mm_Width_1.0mm, B.Cu at (153.6, 138.5)
- added REF**606: Pad_Link_1.7mm_Width_1.0mm, proto-pcb-silks:PadLink_1.7mm_Width_1.0mm, B.Cu at (156.2, 138.5)
- added REF**607: Pad_Link_1.7mm_Width_1.0mm, proto-pcb-silks:PadLink_1.7mm_Width_1.0mm, B.Cu at (158.7, 138.5)
- added REF**608: Pad_Link_1.7mm_Width_1.0mm, proto-pcb-silks:PadLink_1.7mm_Width_1.0mm, B.Cu at (161.3, 138.5)
- added REF**609: Pad_Link_1.7mm_Width_1.0mm, proto-pcb-silks:PadLink_1.7mm_Width_1.0mm, B.Cu at (163.8, 138.5)
- added REF**610: Pad_Link_1.7mm_Width_1.0mm, proto-pcb-silks:PadLink_1.7mm_Width_1.0mm, B.Cu at (166.3, 138.5)
- added REF**611: Pad_Link_1.7mm_Width_1.0mm, proto-pcb-silks:PadLink_1.7mm_Width_1.0mm, B.Cu at (113.0, 141.0)
- added REF**612: Pad_Link_1.7mm_Width_1.0mm, proto-pcb-silks:PadLink_1.7mm_Width_1.0mm, B.Cu at (115.5, 141.0)
- added REF**613: Pad_Link_1.7mm_Width_1.0mm, proto-pcb-silks:PadLink_1.7mm_Width_1.0mm, B.Cu at (118.1, 141.0)
- added REF**614: Pad_Link_1.7mm_Width_1.0mm, proto-pcb-silks:PadLink_1.7mm_Width_1.0mm, B.Cu at (120.6, 141.0)
- added REF**615: Pad_Link_1.7mm_Width_1.0mm, proto-pcb-silks:PadLink_1.7mm_Width_1.0mm, B.Cu at (123.2, 141.0)
- added REF**616: Pad_Link_1.7mm_Width_1.0mm, proto-pcb-silks:PadLink_1.7mm_Width_1.0mm, B.Cu at (125.7, 141.0)
- added REF**617: Pad_Link_1.7mm_Width_1.0mm, proto-pcb-silks:PadLink_1.7mm_Width_1.0mm, B.Cu at (128.2, 141.0)
- added REF**618: Pad_Link_1.7mm_Width_1.0mm, proto-pcb-silks:PadLink_1.7mm_Width_1.0mm, B.Cu at (130.8, 141.0)
- added REF**619: Pad_Link_1.7mm_Width_1.0mm, proto-pcb-silks:PadLink_1.7mm_Width_1.0mm, B.Cu at (133.3, 141.0)
- added REF**620: Pad_Link_1.7mm_Width_1.0mm, proto-pcb-silks:PadLink_1.7mm_Width_1.0mm, B.Cu at (135.9, 141.0)
- added REF**621: Pad_Link_1.7mm_Width_1.0mm, proto-pcb-silks:PadLink_1.7mm_Width_1.0mm, B.Cu at (138.4, 141.0)
- added REF**622: Pad_Link_1.7mm_Width_1.0mm, proto-pcb-silks:PadLink_1.7mm_Width_1.0mm, B.Cu at (113.0, 143.6)
- added REF**623: Pad_Link_1.7mm_Width_1.0mm, proto-pcb-silks:PadLink_1.7mm_Width_1.0mm, B.Cu at (143.5, 141.0)
- added REF**624: Pad_Link_1.7mm_Width_1.0mm, proto-pcb-silks:PadLink_1.7mm_Width_1.0mm, B.Cu at (146.0, 141.0)
- added REF**625: Pad_Link_1.7mm_Width_1.0mm, proto-pcb-silks:PadLink_1.7mm_Width_1.0mm, B.Cu at (148.6, 141.0)
- added REF**626: Pad_Link_1.7mm_Width_1.0mm, proto-pcb-silks:PadLink_1.7mm_Width_1.0mm, B.Cu at (151.1, 141.0)
- added REF**627: Pad_Link_1.7mm_Width_1.0mm, proto-pcb-silks:PadLink_1.7mm_Width_1.0mm, B.Cu at (153.6, 141.0)
- added REF**628: Pad_Link_1.7mm_Width_1.0mm, proto-pcb-silks:PadLink_1.7mm_Width_1.0mm, B.Cu at (156.2, 141.0)
- added REF**629: Pad_Link_1.7mm_Width_1.0mm, proto-pcb-silks:PadLink_1.7mm_Width_1.0mm, B.Cu at (158.7, 141.0)
- added REF**630: Pad_Link_1.7mm_Width_1.0mm, proto-pcb-silks:PadLink_1.7mm_Width_1.0mm, B.Cu at (161.3, 141.0)
- added REF**631: Pad_Link_1.7mm_Width_1.0mm, proto-pcb-silks:PadLink_1.7mm_Width_1.0mm, B.Cu at (163.8, 141.0)
- added REF**632: Pad_Link_1.7mm_Width_1.0mm, proto-pcb-silks:PadLink_1.7mm_Width_1.0mm, B.Cu at (166.3, 141.0)
- added REF**633: Pad_Link_1.7mm_Width_1.0mm, proto-pcb-silks:PadLink_1.7mm_Width_1.0mm, B.Cu at (115.5, 143.6)
- added REF**634: Pad_Link_1.7mm_Width_1.0mm, proto-pcb-silks:PadLink_1.7mm_Width_1.0mm, B.Cu at (118.1, 143.6)
- added REF**635: Pad_Link_1.7mm_Width_1.0mm, proto-pcb-silks:PadLink_1.7mm_Width_1.0mm, B.Cu at (120.6, 143.6)
- added REF**636: Pad_Link_1.7mm_Width_1.0mm, proto-pcb-silks:PadLink_1.7mm_Width_1.0mm, B.Cu at (123.2, 143.6)
- added REF**637: Pad_Link_1.7mm_Width_1.0mm, proto-pcb-silks:PadLink_1.7mm_Width_1.0mm, B.Cu at (125.7, 143.6)
- added REF**638: Pad_Link_1.7mm_Width_1.0mm, proto-pcb-silks:PadLink_1.7mm_Width_1.0mm, B.Cu at (128.2, 143.6)
- added REF**639: Pad_Link_1.7mm_Width_1.0mm, proto-pcb-silks:PadLink_1.7mm_Width_1.0mm, B.Cu at (130.8, 143.6)
- added REF**640: Pad_Link_1.7mm_Width_1.0mm, proto-pcb-silks:PadLink_1.7mm_Width_1.0mm, B.Cu at (133.3, 143.6)
- added REF**641: Pad_Link_1.7mm_Width_1.0mm, proto-pcb-silks:PadLink_1.7mm_Width_1.0mm, B.Cu at (135.9, 143.6)
- added REF**642: Pad_Link_1.7mm_Width_1.0mm, proto-pcb-silks:PadLink_1.7mm_Width_1.0mm, B.Cu at (138.4, 143.6)
- added REF**643: Pad_Link_1.7mm_Width_1.0mm, proto-pcb-silks:PadLink_1.7mm_Width_1.0mm, B.Cu at (140.9, 143.6)
- added REF**644: Pad_Link_1.7mm_Width_1.0mm, proto-pcb-silks:PadLink_1.7mm_Width_1.0mm, B.Cu at (143.5, 143.6)
- added REF**645: Pad_Link_1.7mm_Width_1.0mm, proto-pcb-silks:PadLink_1.7mm_Width_1.0mm, B.Cu at (146.0, 143.6)
- added REF**646: Pad_Link_1.7mm_Width_1.0mm, proto-pcb-silks:PadLink_1.7mm_Width_1.0mm, B.Cu at (148.6, 143.6)
- added REF**647: Pad_Link_1.7mm_Width_1.0mm, proto-pcb-silks:PadLink_1.7mm_Width_1.0mm, B.Cu at (151.1, 143.6)
- added REF**648: Pad_Link_1.7mm_Width_1.0mm, proto-pcb-silks:PadLink_1.7mm_Width_1.0mm, B.Cu at (153.6, 143.6)
- added REF**649: Pad_Link_1.7mm_Width_1.0mm, proto-pcb-silks:PadLink_1.7mm_Width_1.0mm, B.Cu at (156.2, 143.6)
- added REF**650: Pad_Link_1.7mm_Width_1.0mm, proto-pcb-silks:PadLink_1.7mm_Width_1.0mm, B.Cu at (158.7, 143.6)
- added REF**651: Pad_Link_1.7mm_Width_1.0mm, proto-pcb-silks:PadLink_1.7mm_Width_1.0mm, B.Cu at (161.3, 143.6)
- added REF**652: Pad_Link_1.7mm_Width_1.0mm, proto-pcb-silks:PadLink_1.7mm_Width_1.0mm, B.Cu at (163.8, 143.6)
- added REF**653: Pad_Link_1.7mm_Width_1.0mm, proto-pcb-silks:PadLink_1.7mm_Width_1.0mm, B.Cu at (166.3, 143.6)
- added REF**654: Pad_Link_1.7mm_Width_1.0mm, proto-pcb-silks:PadLink_1.7mm_Width_1.0mm, B.Cu at (168.9, 143.6)
- added REF**655: Pad_Link_1.7mm_Width_1.0mm, proto-pcb-silks:PadLink_1.7mm_Width_1.0mm, B.Cu at (113.0, 148.6)
- added REF**661: Pad_Link_1.7mm_Width_1.0mm, proto-pcb-silks:PadLink_1.7mm_Width_1.0mm, B.Cu at (128.2, 148.6)
- added REF**662: Pad_Link_1.7mm_Width_1.0mm, proto-pcb-silks:PadLink_1.7mm_Width_1.0mm, B.Cu at (130.8, 148.6)
- added REF**663: Pad_Link_1.7mm_Width_1.0mm, proto-pcb-silks:PadLink_1.7mm_Width_1.0mm, B.Cu at (133.3, 148.6)
- added REF**664: Pad_Link_1.7mm_Width_1.0mm, proto-pcb-silks:PadLink_1.7mm_Width_1.0mm, B.Cu at (135.9, 148.6)
- added REF**665: Pad_Link_1.7mm_Width_1.0mm, proto-pcb-silks:PadLink_1.7mm_Width_1.0mm, B.Cu at (138.4, 148.6)
- added REF**667: Pad_Link_1.7mm_Width_1.0mm, proto-pcb-silks:PadLink_1.7mm_Width_1.0mm, B.Cu at (143.5, 148.6)
- added REF**668: Pad_Link_1.7mm_Width_1.0mm, proto-pcb-silks:PadLink_1.7mm_Width_1.0mm, B.Cu at (146.0, 148.6)
- added REF**669: Pad_Link_1.7mm_Width_1.0mm, proto-pcb-silks:PadLink_1.7mm_Width_1.0mm, B.Cu at (148.6, 148.6)
- added REF**670: Pad_Link_1.7mm_Width_1.0mm, proto-pcb-silks:PadLink_1.7mm_Width_1.0mm, B.Cu at (151.1, 148.6)
- added REF**671: Pad_Link_1.7mm_Width_1.0mm, proto-pcb-silks:PadLink_1.7mm_Width_1.0mm, B.Cu at (153.6, 148.6)
- added REF**672: Pad_Link_1.7mm_Width_1.0mm, proto-pcb-silks:PadLink_1.7mm_Width_1.0mm, B.Cu at (156.2, 148.6)
- added REF**673: Pad_Link_1.7mm_Width_1.0mm, proto-pcb-silks:PadLink_1.7mm_Width_1.0mm, B.Cu at (158.7, 148.6)
- added REF**675: Pad_Link_1.7mm_Width_1.0mm, proto-pcb-silks:PadLink_1.7mm_Width_1.0mm, B.Cu at (113.0, 151.2)
- added REF**676: Pad_Link_1.7mm_Width_1.0mm, proto-pcb-silks:PadLink_1.7mm_Width_1.0mm, B.Cu at (113.0, 153.7)
- added REF**677: Pad_Link_1.7mm_Width_1.0mm, proto-pcb-silks:PadLink_1.7mm_Width_1.0mm, B.Cu at (115.5, 153.7)
- added REF**681: Pad_Link_1.7mm_Width_1.0mm, proto-pcb-silks:PadLink_1.7mm_Width_1.0mm, B.Cu at (128.2, 151.2)
- added REF**682: Pad_Link_1.7mm_Width_1.0mm, proto-pcb-silks:PadLink_1.7mm_Width_1.0mm, B.Cu at (130.8, 151.2)
- added REF**683: Pad_Link_1.7mm_Width_1.0mm, proto-pcb-silks:PadLink_1.7mm_Width_1.0mm, B.Cu at (133.3, 151.2)
- added REF**684: Pad_Link_1.7mm_Width_1.0mm, proto-pcb-silks:PadLink_1.7mm_Width_1.0mm, B.Cu at (135.9, 151.2)
- added REF**685: Pad_Link_1.7mm_Width_1.0mm, proto-pcb-silks:PadLink_1.7mm_Width_1.0mm, B.Cu at (138.4, 151.2)
- added REF**687: Pad_Link_1.7mm_Width_1.0mm, proto-pcb-silks:PadLink_1.7mm_Width_1.0mm, B.Cu at (143.5, 151.2)
- added REF**688: Pad_Link_1.7mm_Width_1.0mm, proto-pcb-silks:PadLink_1.7mm_Width_1.0mm, B.Cu at (146.0, 151.2)
- added REF**689: Pad_Link_1.7mm_Width_1.0mm, proto-pcb-silks:PadLink_1.7mm_Width_1.0mm, B.Cu at (148.6, 151.2)
- added REF**690: Pad_Link_1.7mm_Width_1.0mm, proto-pcb-silks:PadLink_1.7mm_Width_1.0mm, B.Cu at (151.1, 151.2)
- added REF**691: Pad_Link_1.7mm_Width_1.0mm, proto-pcb-silks:PadLink_1.7mm_Width_1.0mm, B.Cu at (153.6, 151.2)
- added REF**692: Pad_Link_1.7mm_Width_1.0mm, proto-pcb-silks:PadLink_1.7mm_Width_1.0mm, B.Cu at (156.2, 151.2)
- added REF**693: Pad_Link_1.7mm_Width_1.0mm, proto-pcb-silks:PadLink_1.7mm_Width_1.0mm, B.Cu at (158.7, 151.2)
- added REF**694: Pad_Link_1.7mm_Width_1.0mm, proto-pcb-silks:PadLink_1.7mm_Width_1.0mm, B.Cu at (128.2, 153.7)
- added REF**695: Pad_Link_1.7mm_Width_1.0mm, proto-pcb-silks:PadLink_1.7mm_Width_1.0mm, B.Cu at (130.8, 153.7)
- added REF**696: Pad_Link_1.7mm_Width_1.0mm, proto-pcb-silks:PadLink_1.7mm_Width_1.0mm, B.Cu at (133.3, 153.7)
- added REF**697: Pad_Link_1.7mm_Width_1.0mm, proto-pcb-silks:PadLink_1.7mm_Width_1.0mm, B.Cu at (135.9, 153.7)
- added REF**698: Pad_Link_1.7mm_Width_1.0mm, proto-pcb-silks:PadLink_1.7mm_Width_1.0mm, B.Cu at (138.4, 153.7)
- added REF**699: Pad_Link_1.7mm_Width_1.0mm, proto-pcb-silks:PadLink_1.7mm_Width_1.0mm, B.Cu at (140.9, 153.7)
- added REF**700: Pad_Link_1.7mm_Width_1.0mm, proto-pcb-silks:PadLink_1.7mm_Width_1.0mm, B.Cu at (143.5, 153.7)
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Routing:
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
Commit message: Created gerber files for single board
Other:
- rule pad_to_mask_clearance: 0.051 -> 0
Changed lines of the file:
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@@
   )
   (setup
-    (pad_to_mask_clearance 0.051)
-    (solder_mask_min_width 0.25)
+    (pad_to_mask_clearance 0)
     (pcbplotparams
       (layerselection 0x00010f0_ffffffff)
-      (plot_on_all_layers_selection 0x0000000_00000000)
+      (plot_on_all_layers_selection 0x0001000_00000000)
       (disableapertmacros false)
       (usegerberextensions false)
